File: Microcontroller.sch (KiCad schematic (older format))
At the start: 36 parts, among them CN2 CONN_RCPT_USB2.0_MINI_B_SMD_R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, Q10 2N7002BK, U2 STM32L476RGLQFP64, X1 ABM3B-16.000MHZ

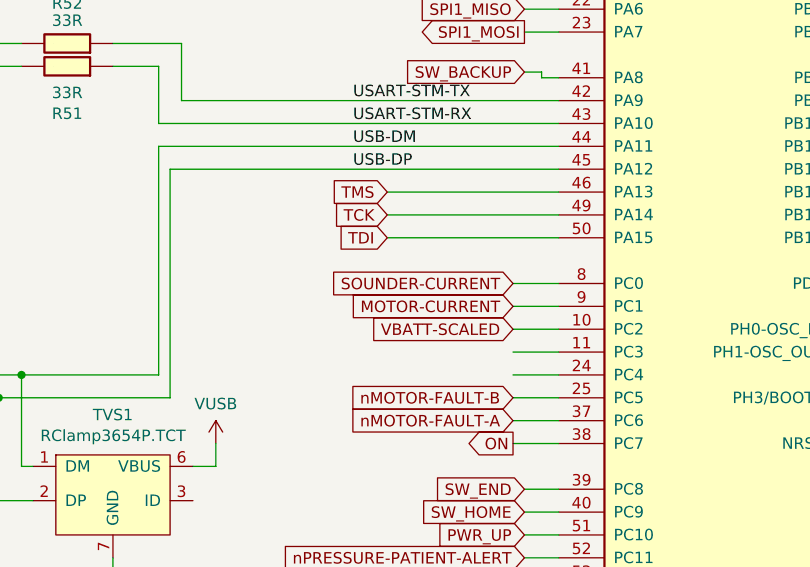
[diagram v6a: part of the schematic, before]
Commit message: Moved SOUNDER-CURRENT input signal from MCU to FPGA
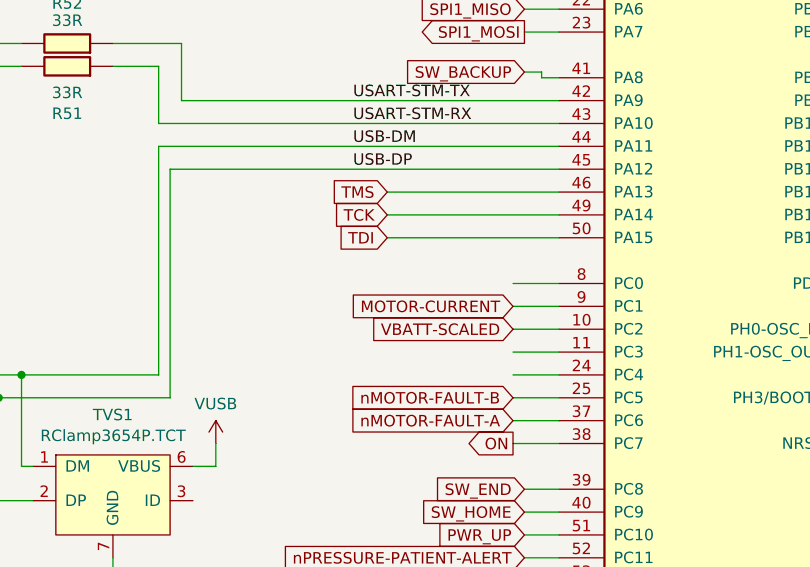
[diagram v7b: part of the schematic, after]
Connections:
- net labels removed: SOUNDER-CURRENT
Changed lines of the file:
@@
 Text GLabel 6550 3100 2    50   Output ~ 0
 CE-CONTROL
-Text GLabel 4750 3400 0    50   Input ~ 0
-SOUNDER-CURRENT
 Text Label 3850 1900 0    50   ~ 0
 ANALOG-SPARE

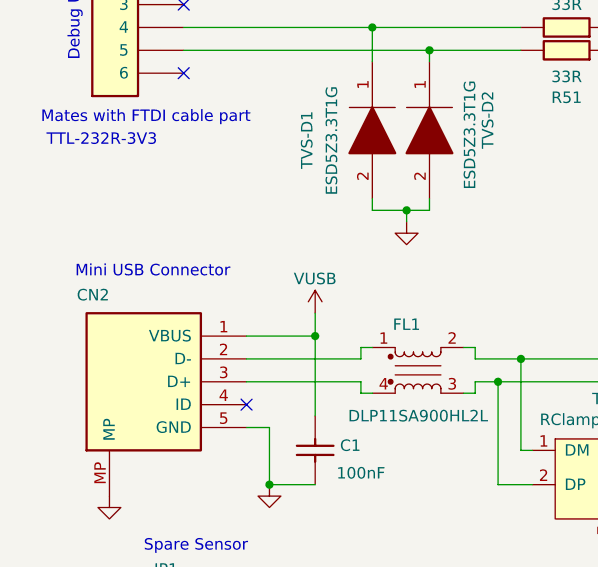
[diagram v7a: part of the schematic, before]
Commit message: Replaced Mini USB connector on MCU sheet with Micro-B USB. Added VUSB label to power supply 3V3 always on circuit.
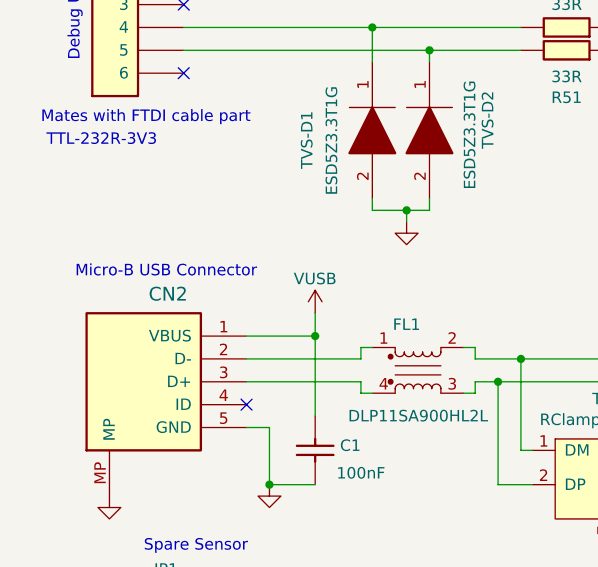
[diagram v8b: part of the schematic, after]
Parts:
- removed CN2: CONN_RCPT_USB2.0_MINI_B_SMD_R_A, symbol OpenVent:CONN_RCPT_USB2.0_MINI_B_SMD_R_A
- added CN2: CONN_RCPT_USB2.0_MICRO_B_SMD_R_A, symbol OpenVent:CONN_RCPT_USB2.0_MICRO_B_SMD_R_A
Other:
- note added: "Micro-B USB Connector"
- note removed: "Mini USB Connector"
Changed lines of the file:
@@
-$EndComp
-$Comp
-L OpenVent:CONN_RCPT_USB2.0_MINI_B_SMD_R_A CN2
-U 1 1 5F8DD141
-P 1400 4100
-F 0 "CN2" H 2000 4650 50  0000 L BNN
-F 1 "CONN_RCPT_USB2.0_MINI_B_SMD_R_A" H 1950 4300 50  0001 C CNN
-F 2 "" H 1400 4100 50  0001 C CNN
-F 3 "" H 1400 4100 50  0001 C CNN
-	1    1400 4100
-	-1   0    0    -1
 $EndComp
 $Comp
@@
 Connection ~ 8175 6175
 Text Notes 650  3450 0    50   ~ 0
-Mini USB Connector
+Micro-B USB Connector
 Connection ~ 3975 6325
 Wire Wire Line
@@
 Text GLabel 4750 4100 0    50   Output ~ 0
 ON
+$Comp
+L OpenVent:CONN_RCPT_USB2.0_MICRO_B_SMD_R_A CN2
+U 1 1 60722C2F
+P 1400 4100
+F 0 "CN2" H 1743 4683 60  0000 C CNN
+F 1 "CONN_RCPT_USB2.0_MICRO_B_SMD_R_A" H 1743 4789 60  0001 C CNN
+F 2 "" H 1600 4600 60  0001 C CNN
+F 3 "https://drive.google.com/drive/u/1/folders/1bT0MezjjDfDXdTdQktjf6O5y5oTJs8ND" H 1743 4683 60  0001 C CNN
+	1    1400 4100
+	-1   0    0    -1
+$EndComp
 $EndSCHEMATC
